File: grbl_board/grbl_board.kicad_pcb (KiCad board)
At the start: 4 copper layers, 138.4 x 138.3 mm, 242 parts, among them J1 COOL, J10 DOOR, J11 PROBE, J12 INP, J13 LIM, J14 24V_VFD, J15 Spindle, J16 freq, J17 USB_B, J18 ICSP, J2 12VDC, J3 USB_B, J4 ICSP, J5 Screw_Terminal_01x04, J6 X_STEPPER, J7 Y_STEPPER, J8 Z_STEPPER, J9 E_STEPPER, Q1 BSS127S, Q2 BSS127S, Q3 ZVN4306GTA, Q4 IRF9Z24SPBF, Q5 BSS127S, Q6 BSS127S, Q7 BSS127S, SW1 SW_Push, SW2 SW_Push, U1 FT231XS, U10 6N137, U11 6N137, U12 6N137, U13 6N137, U14 6N137, U15 6N137, U16 6N137, U17 6N137, U18 6N137, U19 6N137, U2 ATmega2560-16AU, U20 6N137, U21 BD9G341EFJ, U22 LMV358, U23 OPA2192, U24 L7805, U25 FT231XS, U26 40106, U27 74LS155, U28 ATmega328P-AU, U29 74LS153, U3 LT1962-5, U30 74LS153, U4 BD9G341EFJ, U5 TMC5160_SILENTSTEPSTICK, U6 TMC5160_SILENTSTEPSTICK, U7 TMC5160_SILENTSTEPSTICK, U8 TMC5160_SILENTSTEPSTICK, U9 6N137, Y1 16M, Y2 16M

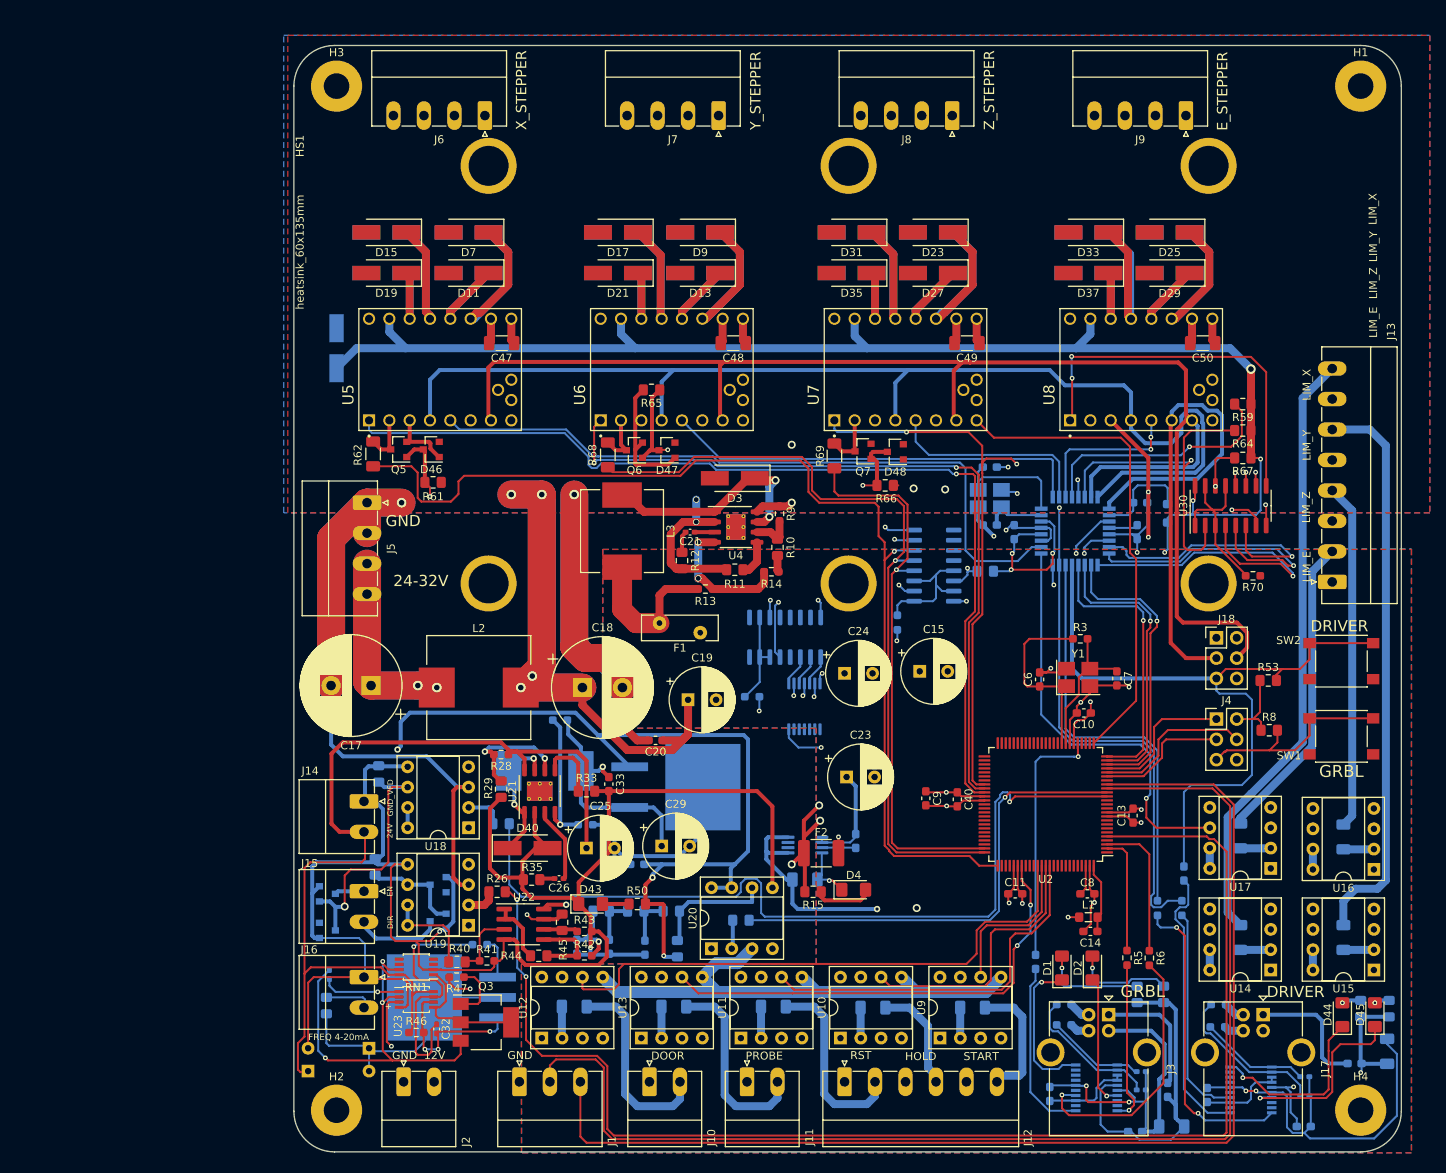
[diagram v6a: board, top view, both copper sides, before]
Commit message: fixed pullup resistors on board, and 5v regulator overheating, and stepper driver flipped
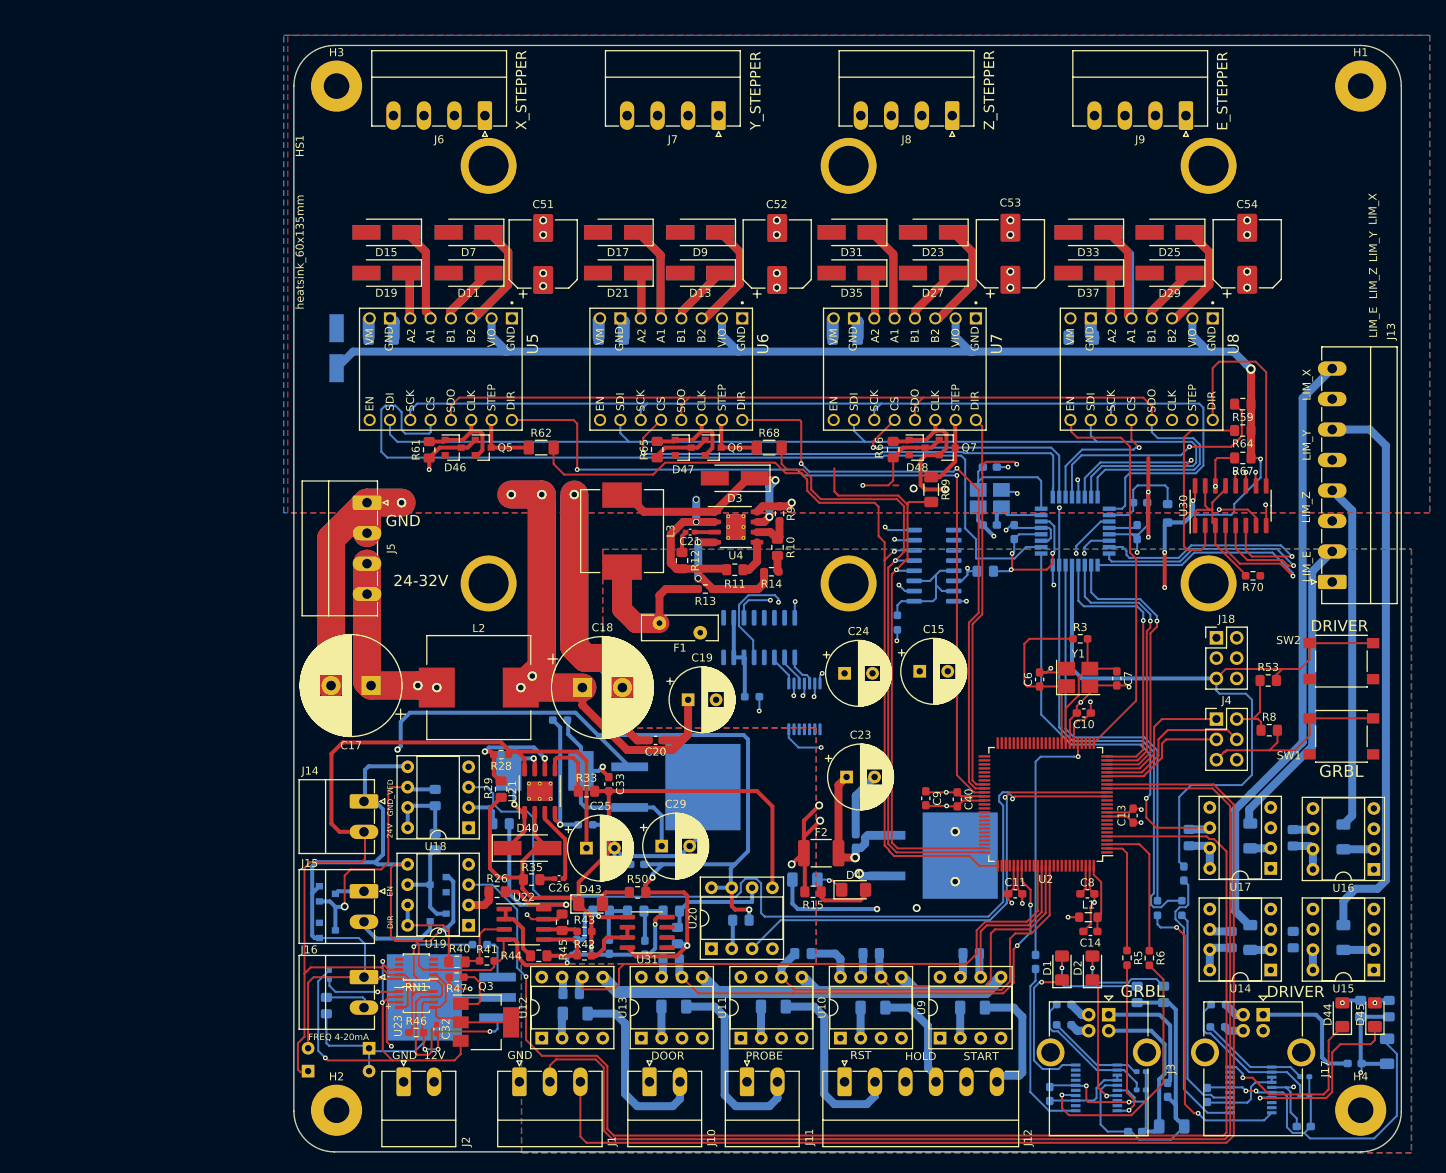
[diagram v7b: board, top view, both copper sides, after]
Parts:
- added C51: 100u, Capacitor_SMD:CP_Elec_8x10, F.Cu at (104.0, 48.8)
- added C52: 100u, Capacitor_SMD:CP_Elec_8x10, F.Cu at (133.2, 48.8)
- added C53: 100u, Capacitor_SMD:CP_Elec_8x10, F.Cu at (162.4, 48.8)
- added C54: 100u, Capacitor_SMD:CP_Elec_8x10, F.Cu at (192.0, 48.8)
- added R71: 1k, Resistor_SMD:R_0805_2012Metric_Pad1.15x1.40mm_HandSolder, B.Cu at (136.5, 136.2)
- added R72: 1k, Resistor_SMD:R_0805_2012Metric_Pad1.15x1.40mm_HandSolder, B.Cu at (107.5, 141.2)
- added R73: 1k, Resistor_SMD:R_0805_2012Metric_Pad1.15x1.40mm_HandSolder, B.Cu at (120.0, 137.0)
- added R74: 1k, Resistor_SMD:R_0805_2012Metric_Pad1.15x1.40mm_HandSolder, B.Cu at (190.0, 134.5)
- added R75: 1k, Resistor_SMD:R_0805_2012Metric_Pad1.15x1.40mm_HandSolder, B.Cu at (197.8, 134.5)
- added R76: 1k, Resistor_SMD:R_0805_2012Metric_Pad1.15x1.40mm_HandSolder, B.Cu at (197.8, 121.8)
- added R77: 1k, Resistor_SMD:R_0805_2012Metric_Pad1.15x1.40mm_HandSolder, B.Cu at (184.8, 121.8)
- added R78: 1k, Resistor_SMD:R_0805_2012Metric_Pad1.15x1.40mm_HandSolder, B.Cu at (90.5, 116.8)
- added R79: 1k, Resistor_SMD:R_0805_2012Metric_Pad1.15x1.40mm_HandSolder, B.Cu at (90.5, 122.2)
- added U31: LMV358, Package_SO:SOIC-8_3.9x4.9mm_P1.27mm, F.Cu at (117.0, 133.6)
- C47, C48, C49, C50: moved to B.Cu
- R30, R31, R32, R34, R36, R39: value 10k -> 1k
- U3: value LT1962-5 -> L7805; footprint Package_SO:MSOP-8_3x3mm_P0.65mm -> Package_TO_SOT_SMD:TO-263-2
- moved R31 77.4 mm to (157.5, 136.2), turned to 180 degrees
- moved C50 73.9 mm to (112.5, 59.2), turned to 0 degrees
- moved C49 73.2 mm to (83.8, 59.2), turned to 0 degrees
- moved C47 72.4 mm to (171.2, 59.2), turned to 0 degrees
- moved R32 62.9 mm to (145.0, 136.2), turned to 180 degrees
- moved R62 21.0 mm to (103.8, 73.0), turned to 0 degrees
- moved R68 20.2 mm to (132.2, 73.0), turned to 0 degrees
- moved U3 16.1 mm to (152.8, 124.0), turned to 0 degrees
- moved C48 14.0 mm to (141.8, 59.2), turned to 0 degrees
- moved R69 12.8 mm to (152.5, 78.2)
- moved Q5 10.6 mm to (96.5, 73.0), turned to 0 degrees
- moved Q7 10.5 mm to (154.5, 73.0), turned to 0 degrees
- moved Q6 9.85 mm to (125.2, 73.0), turned to 0 degrees
- moved R65 7.50 mm to (118.2, 73.2), turned to 90 degrees
- moved R66 4.58 mm to (147.8, 73.2), turned to 90 degrees
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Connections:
- C22 pad 1: Net-(C22-Pad1) -> GND
- C23 pad 1: Net-(C22-Pad1) -> Net-(C22-Pad2)
- F2 pad 2: Net-(C22-Pad1) -> Net-(C22-Pad2)
- R25 pad 2: /grbl_controller/SPINDLE_EN -> /spindle_cntrl/5V
- R26 pad 2: /grbl_controller/SPINDLE_DIR -> /spindle_cntrl/5V
- R27 pad 2: /grbl_controller/SPINDLE_PWM -> /spindle_cntrl/5V
- R31 pad 1: Net-(D38-Pad1) -> /START
- R31 pad 2: /spindle_cntrl/GND_VFD -> +5V
- R32 pad 1: Net-(D39-Pad1) -> /HOLD
- R32 pad 2: /spindle_cntrl/GND_VFD -> +5V
- R42 pad 2: Net-(C30-Pad1) -> Net-(R42-Pad2)
- U18 pad 3: GND -> /grbl_controller/SPINDLE_EN
- U19 pad 3: GND -> /grbl_controller/SPINDLE_DIR
- U20 pad 3: GND -> /grbl_controller/SPINDLE_PWM
- U3 pad 1: Net-(C22-Pad1) -> +12V
- U3 pad 2: Net-(C22-Pad1) -> GND
- U5 pad JP2_3: Net-(D6-Pad2) -> Net-(D18-Pad2)
- U5 pad JP2_4: Net-(D10-Pad2) -> Net-(D14-Pad2)
- U5 pad JP2_5: Net-(D14-Pad2) -> Net-(D10-Pad2)
- U5 pad JP2_6: Net-(D18-Pad2) -> Net-(D6-Pad2)
- U6 pad JP2_3: Net-(D8-Pad2) -> Net-(D20-Pad2)
- U6 pad JP2_4: Net-(D12-Pad2) -> Net-(D16-Pad2)
- U6 pad JP2_5: Net-(D16-Pad2) -> Net-(D12-Pad2)
- U6 pad JP2_6: Net-(D20-Pad2) -> Net-(D8-Pad2)
- U7 pad JP2_3: Net-(D22-Pad2) -> Net-(D34-Pad2)
- U7 pad JP2_4: Net-(D26-Pad2) -> Net-(D30-Pad2)
- U7 pad JP2_5: Net-(D30-Pad2) -> Net-(D26-Pad2)
- U7 pad JP2_6: Net-(D34-Pad2) -> Net-(D22-Pad2)
- U8 pad JP2_3: Net-(D24-Pad2) -> Net-(D36-Pad2)
- U8 pad JP2_4: Net-(D28-Pad2) -> Net-(D32-Pad2)
- U8 pad JP2_5: Net-(D32-Pad2) -> Net-(D28-Pad2)
- U8 pad JP2_6: Net-(D36-Pad2) -> Net-(D24-Pad2)
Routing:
- net /spindle_cntrl/5V: track 161.5 -> 207.7 mm, vias 4 -> 5
- net +5V: track 264.4 -> 298.5 mm, vias 17 -> 18
- net GND: track 719.3 -> 685.9 mm, vias 31 -> 41
- net /grbl_controller/STEP_X: track 136.1 -> 109.4 mm
- net /MISO: track 195.7 -> 171.8 mm
- net /CS_X: track 87.9 -> 111.3 mm
- net /grbl_controller/STEP_Y: track 100.2 -> 78.3 mm
- net /grbl_controller/DIR_Y: track 136.0 -> 115.1 mm
- net /grbl_controller/DIR_X: track 163.6 -> 144.1 mm, vias 2 -> 3
- net /stepper_drivers/E_DIR: track 47.5 -> 28.3 mm, vias 2 -> 0
- net /grbl_controller/DIR_Z: track 100.1 -> 81.8 mm, vias 3 -> 2
- net Net-(C22-Pad1): track 16.8 -> 0.00 mm, vias 1 -> 0
- net Net-(C22-Pad2): track 4.32 -> 20.6 mm, vias 0 -> 1
- net /stepper_drivers/EN: track 154.1 -> 140.9 mm
- net /MOSI: track 178.9 -> 191.2 mm
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
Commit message: moved connectors further out
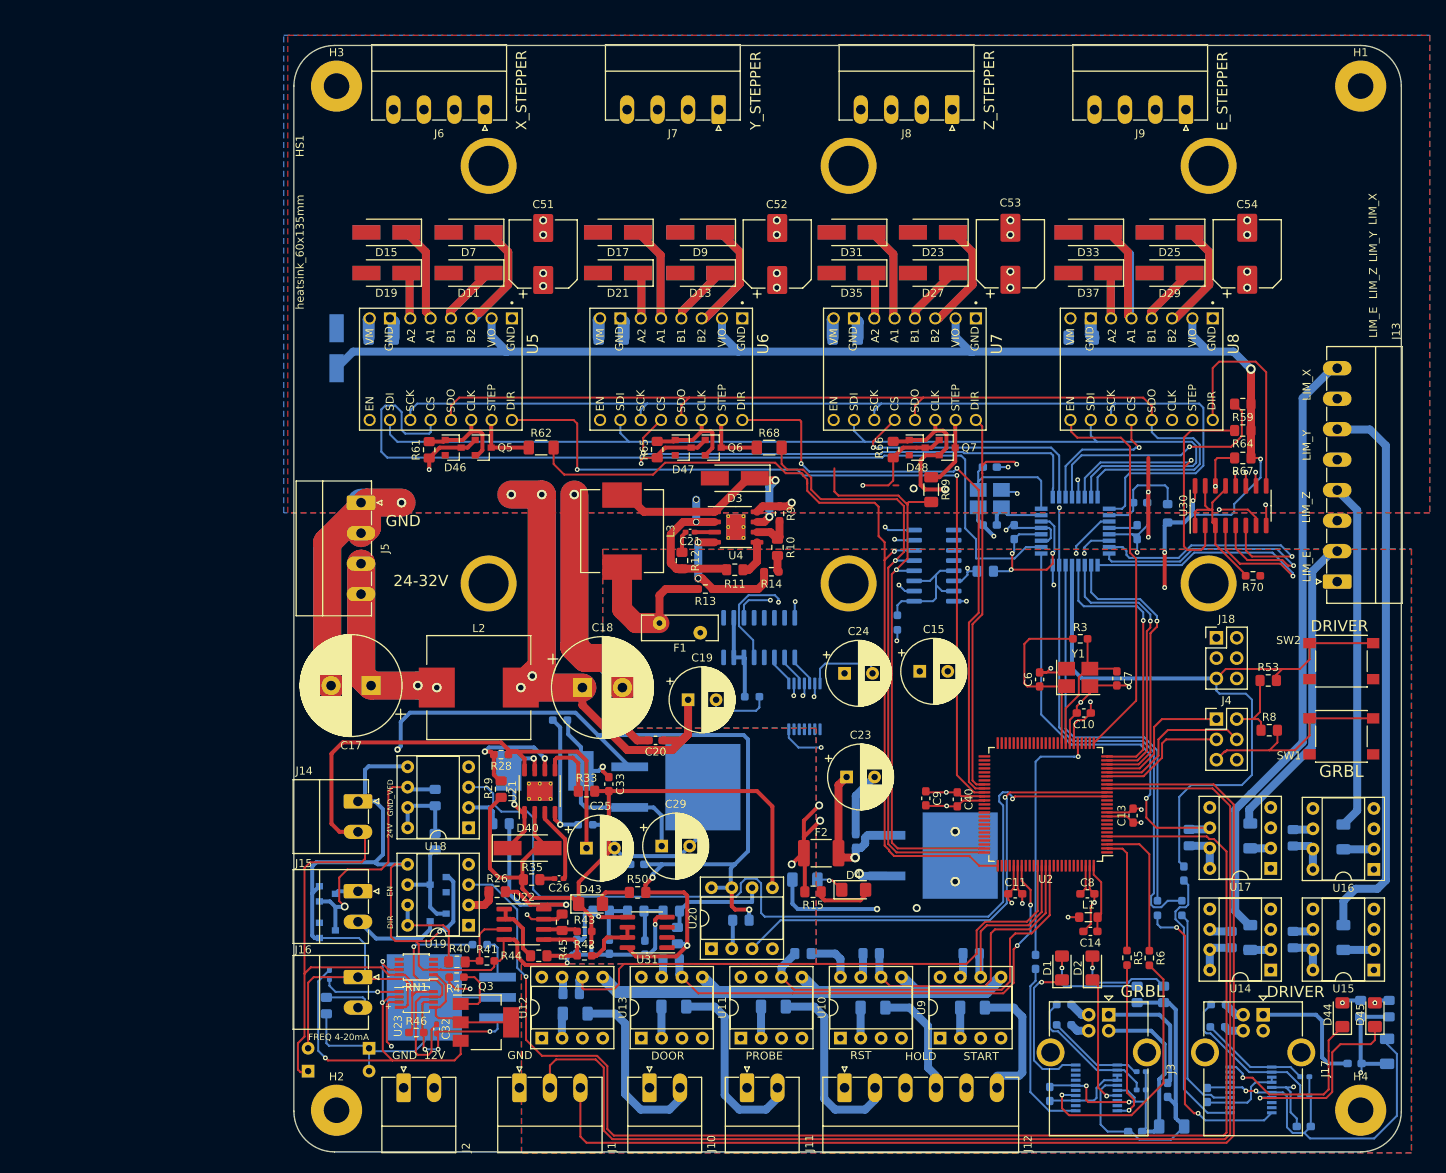
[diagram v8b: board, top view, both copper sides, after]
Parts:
- moved J1 0.75 mm to (101.0, 153.0)
- moved J10 0.75 mm to (117.3, 153.0)
- moved J11 0.75 mm to (129.5, 153.0)
- moved J12 0.75 mm to (141.7, 153.0)
- moved J14 0.75 mm to (80.8, 117.2)
- moved J15 0.75 mm to (80.8, 128.5)
- moved J16 0.75 mm to (80.8, 139.2)
- moved J2 0.75 mm to (86.6, 153.0)
- moved J5 0.75 mm to (81.2, 79.9)
- moved J6 0.75 mm to (96.7, 30.7)
- moved J7 0.75 mm to (125.9, 30.7)
- moved J8 0.75 mm to (155.1, 30.7)
- moved J9 0.75 mm to (184.3, 30.7)
- moved J13 0.62 mm to (203.2, 89.8)
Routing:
- net +12V: track 374.6 -> 344.7 mm
- net GND: track 685.9 -> 704.7 mm, vias 41 -> 39
- net /aux_mcu/Y_EN: track 55.5 -> 58.9 mm, vias 1 -> 2
- net /aux_mcu/LIM_Y: track 84.0 -> 86.5 mm
- net +5V: track 298.5 -> 301.0 mm
- net Net-(J12-Pad2): track 24.1 -> 26.3 mm
- net Net-(C17-Pad1): track 92.0 -> 93.2 mm
- net Net-(D38-Pad1): track 31.5 -> 32.3 mm
